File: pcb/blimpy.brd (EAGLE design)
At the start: 250 x 167 mm, 76 parts, among them J1 MICRO-USB, J4 3-PIN SMD, J5 3-PIN SMD, J6 3-PIN SMD, J7 3-PIN SMD, Q1 mmbt2222, Q2 mmbt2222, Q3 DMG3415U, U1 RGB, U10 MAX17048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

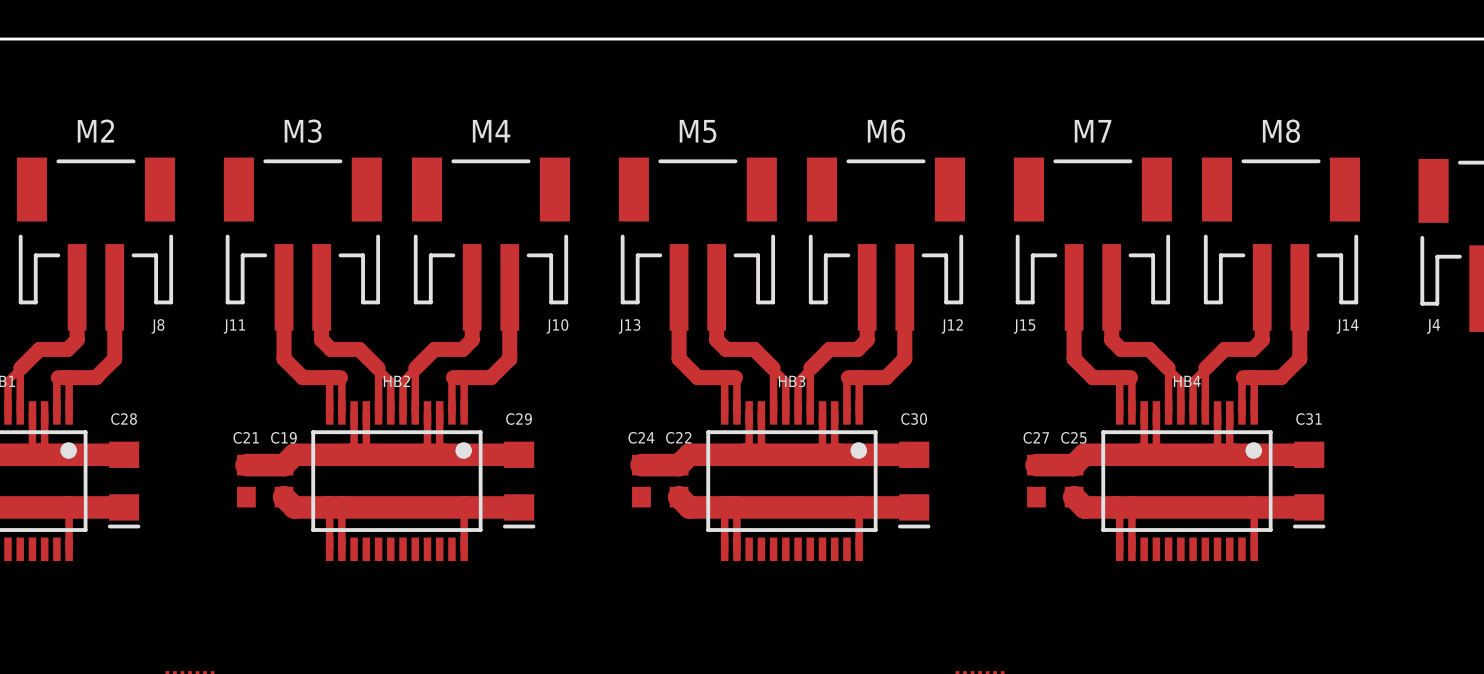
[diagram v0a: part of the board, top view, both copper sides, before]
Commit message: connected adjacent bridges
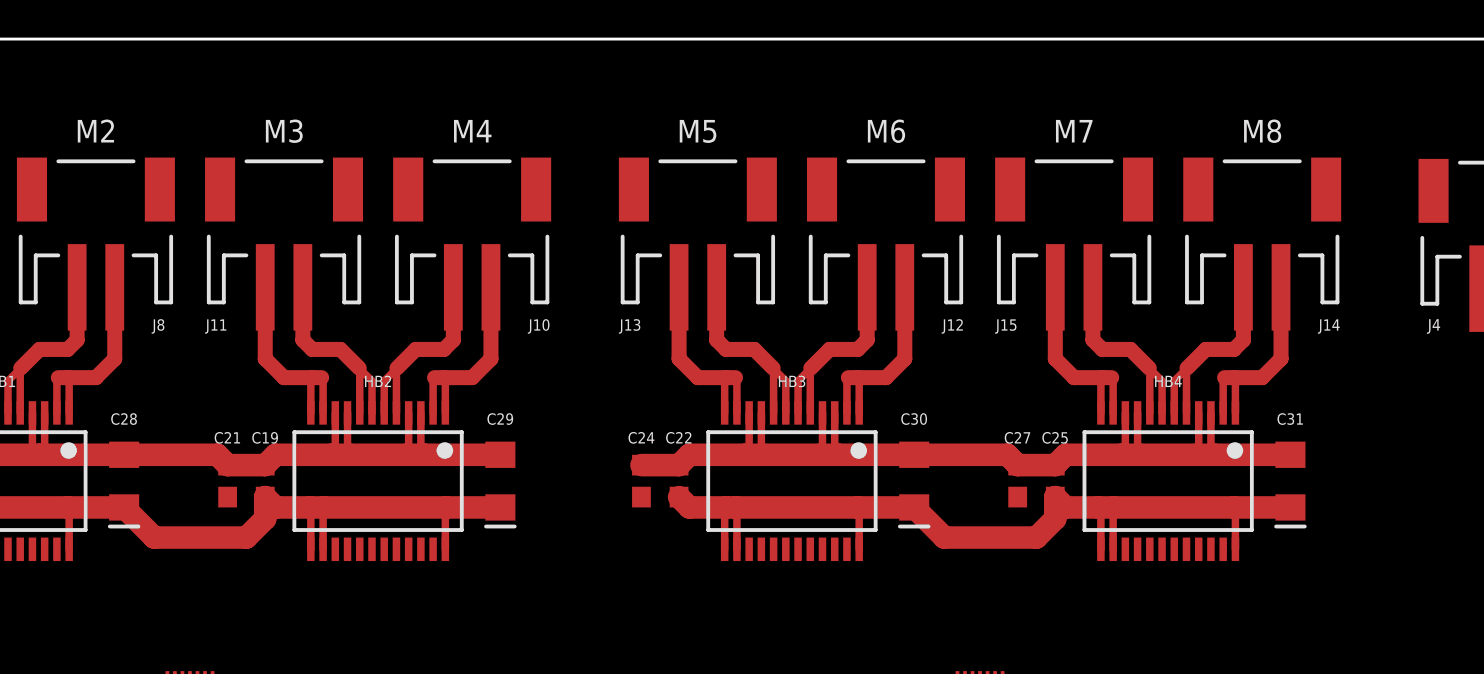
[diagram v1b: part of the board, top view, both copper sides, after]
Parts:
- moved C19 1.00 mm to (55.5, 143.5)
- moved C21 1.00 mm to (53.5, 143.5)
- moved C25 1.00 mm to (97.5, 143.5)
- moved C27 1.00 mm to (95.5, 143.5)
- moved C29 1.00 mm to (68.0, 143.5)
- moved C31 1.00 mm to (110.0, 143.5)
- moved HB2 1.00 mm to (61.5, 143.5)
- moved HB4 1.00 mm to (103.5, 143.5)
- moved J10 1.00 mm to (66.5, 157.5)
- moved J11 1.00 mm to (56.5, 157.5)
- moved J14 1.00 mm to (108.5, 157.5)
- moved J15 1.00 mm to (98.5, 157.5)
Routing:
- net V_BATT: track 77.9 -> 97.4 mm
- net GND: track 95.8 -> 107.3 mm
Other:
- board text added: "Trace Widths for 1oz Copper: Logic: 0.4mm, 15mil (1A) Actors: 0.8mm, 30mil (2A) Battery: 1.2mm, 60mil (3A) Text Sizes Vector, 0.6, 15%"
- board text removed: "Trace Widths for 1oz Copper: Logic: 0.4mm, 15mil (1A) Actors: 0.8mm, 30mil (2A) HBridge: 1.2mm, 45mil (3A) Battery: 1.6mm, 60mil (4A) Text Sizes Vector, 0.6, 15%"

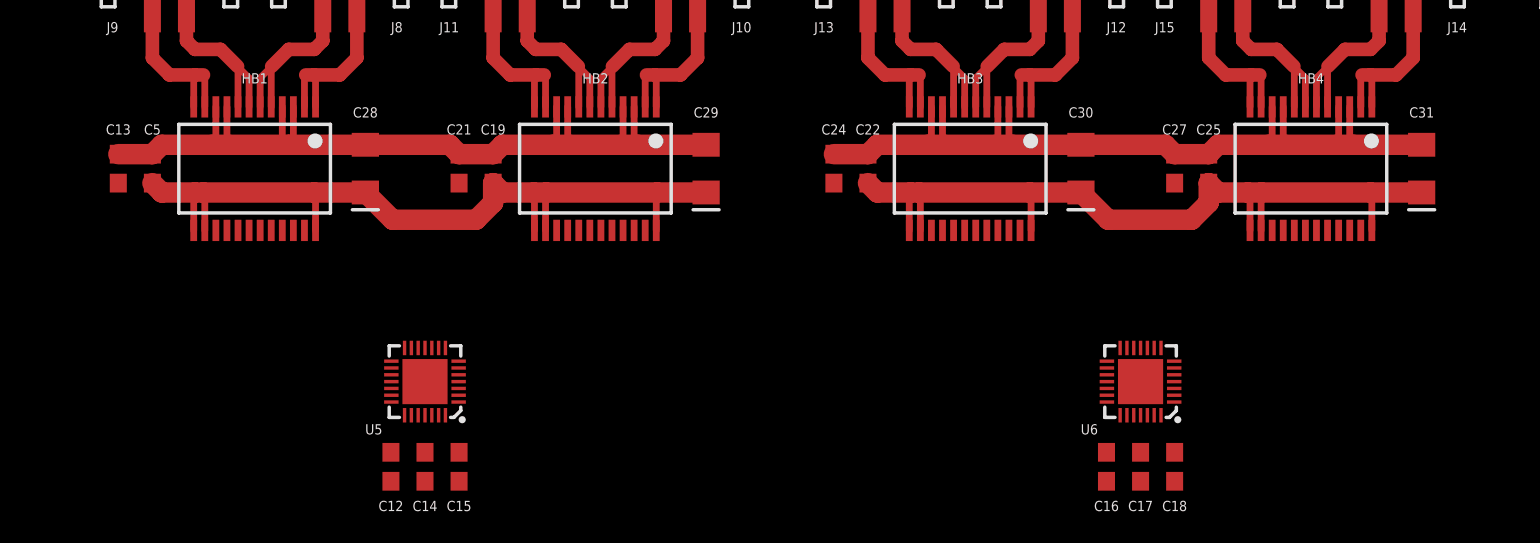
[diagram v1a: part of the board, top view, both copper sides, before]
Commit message: updated hbridge traces and prepared expander
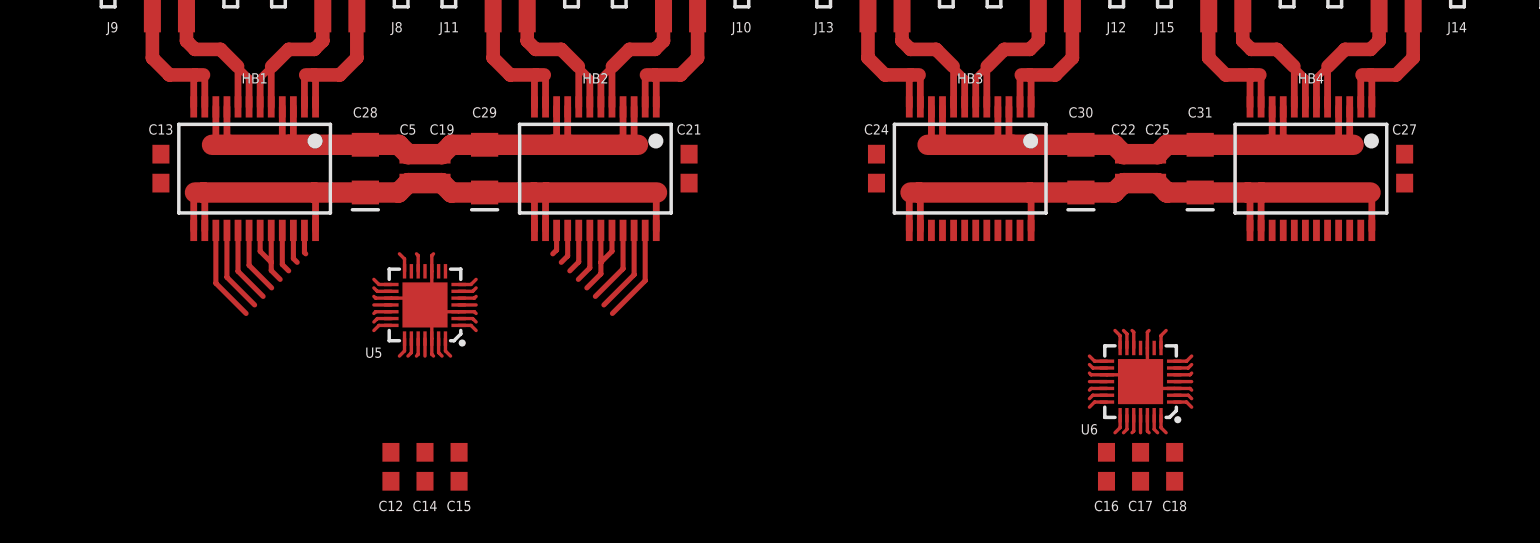
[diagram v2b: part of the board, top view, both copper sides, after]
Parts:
- moved C22 15.0 mm to (92.5, 143.5)
- moved C5 15.0 mm to (50.5, 143.5)
- moved C21 13.5 mm to (67.0, 143.5)
- moved C27 13.5 mm to (109.0, 143.5)
- moved C29 13.0 mm to (55.0, 143.5)
- moved C31 13.0 mm to (97.0, 143.5)
- moved U5 4.50 mm to (51.5, 135.5)
- moved C19 3.00 mm to (52.5, 143.5)
- moved C25 3.00 mm to (94.5, 143.5)
- moved C13 2.50 mm to (36.0, 143.5)
- moved C24 2.50 mm to (78.0, 143.5)
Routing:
- net 3.3V: track 0.00 -> 18.4 mm
- net V_BATT: track 97.4 -> 82.1 mm
- net GND: track 107.3 -> 116.8 mm
- net H2-1: track 0.00 -> 5.67 mm
- net H1-6: track 0.00 -> 5.61 mm
- net H2-2: track 0.00 -> 5.11 mm
- net H1-5: track 0.00 -> 5.05 mm
- net H2-3: track 0.00 -> 4.55 mm
- net H1-4: track 0.00 -> 4.49 mm
- net H2-4: track 0.00 -> 2.59 mm
- net H1-3: track 0.00 -> 2.53 mm
- net SDA: track 0.00 -> 2.13 mm
- net SCL: track 0.00 -> 2.05 mm
- net H2-5: track 0.00 -> 2.03 mm
- net H1-2: track 0.00 -> 1.97 mm
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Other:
- board text added: "Min Trace: 6mil Min Space: 6mil Min Hole: 0.3mm"

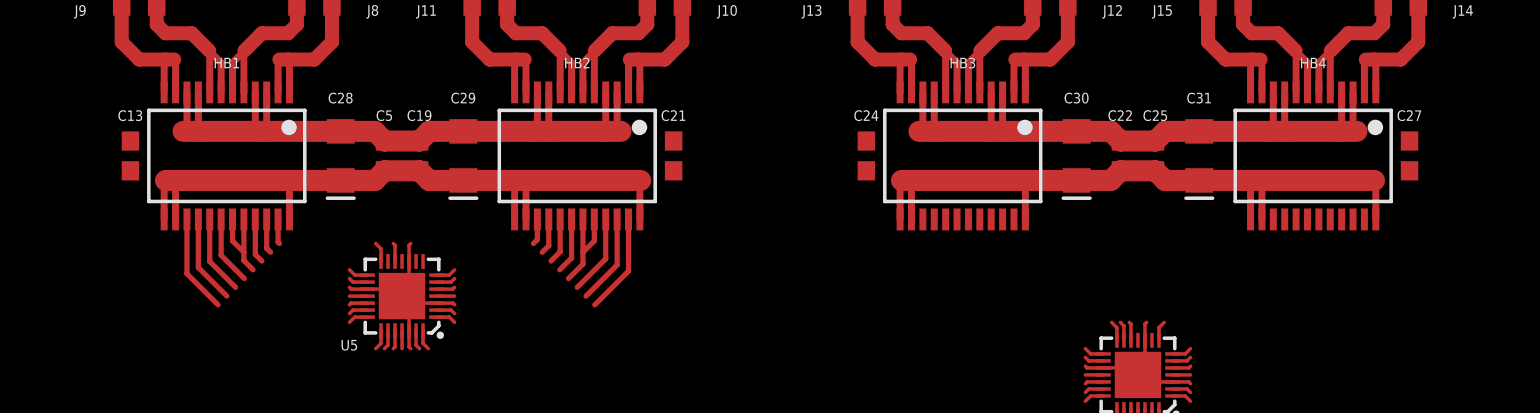
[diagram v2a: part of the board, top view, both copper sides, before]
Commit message: use 0.2mm traces
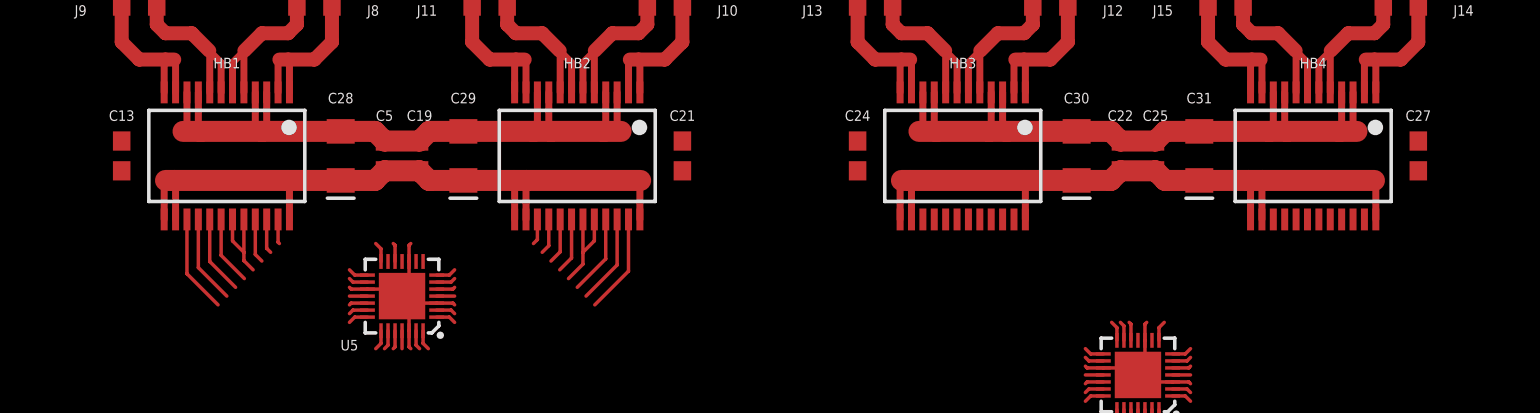
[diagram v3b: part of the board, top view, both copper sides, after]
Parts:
- moved C13 0.50 mm to (35.5, 143.5)
- moved C21 0.50 mm to (67.5, 143.5)
- moved C24 0.50 mm to (77.5, 143.5)
- moved C27 0.50 mm to (109.5, 143.5)
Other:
- board text added: "Trace Widths for 1oz Copper: Logic: 0.2mm, ~8mil Power: 0.4mm, 15mil (1A) Actors: 0.8mm, 30mil (2A) Battery: 1.2mm, 60mil (3A) Text Sizes Vector, 0.6, 15%"
- board text removed: "Trace Widths for 1oz Copper: Logic: 0.4mm, 15mil (1A) Actors: 0.8mm, 30mil (2A) Battery: 1.2mm, 60mil (3A) Text Sizes Vector, 0.6, 15%"

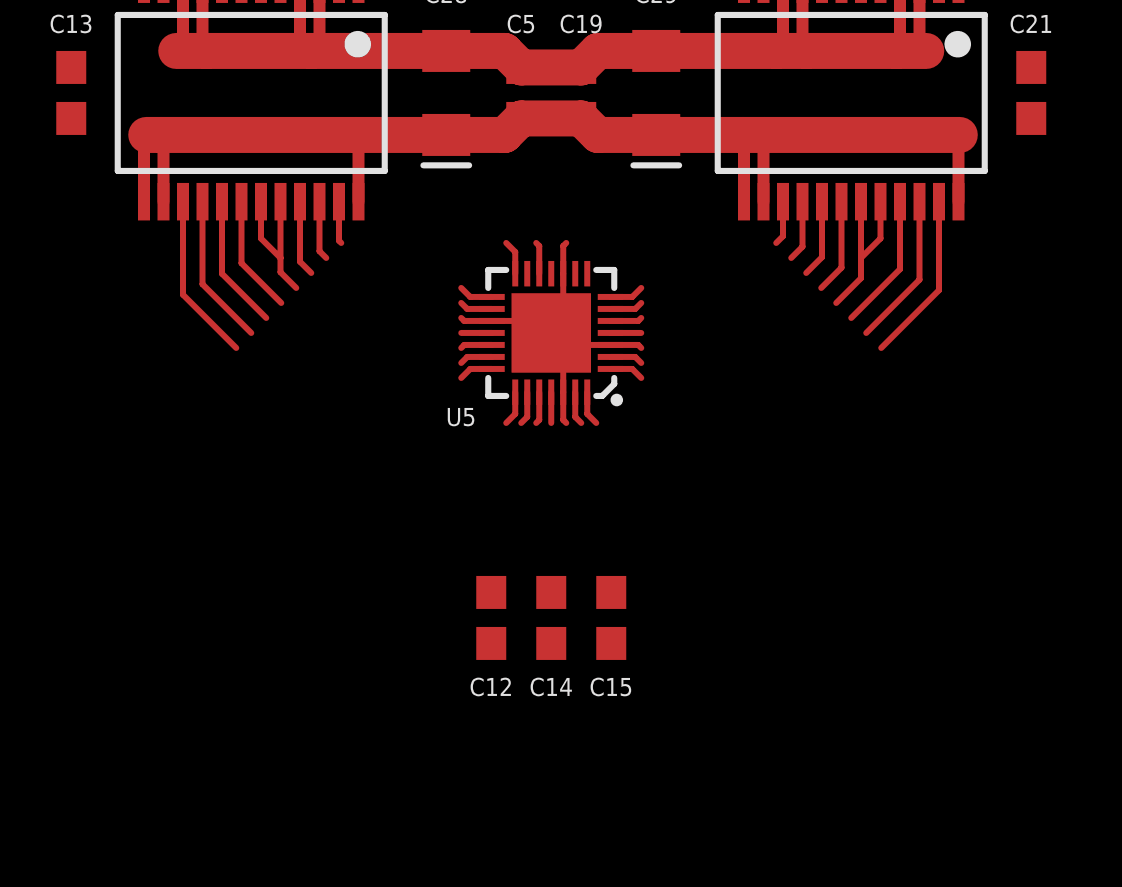
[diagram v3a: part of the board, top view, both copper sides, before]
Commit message: wired io and caps
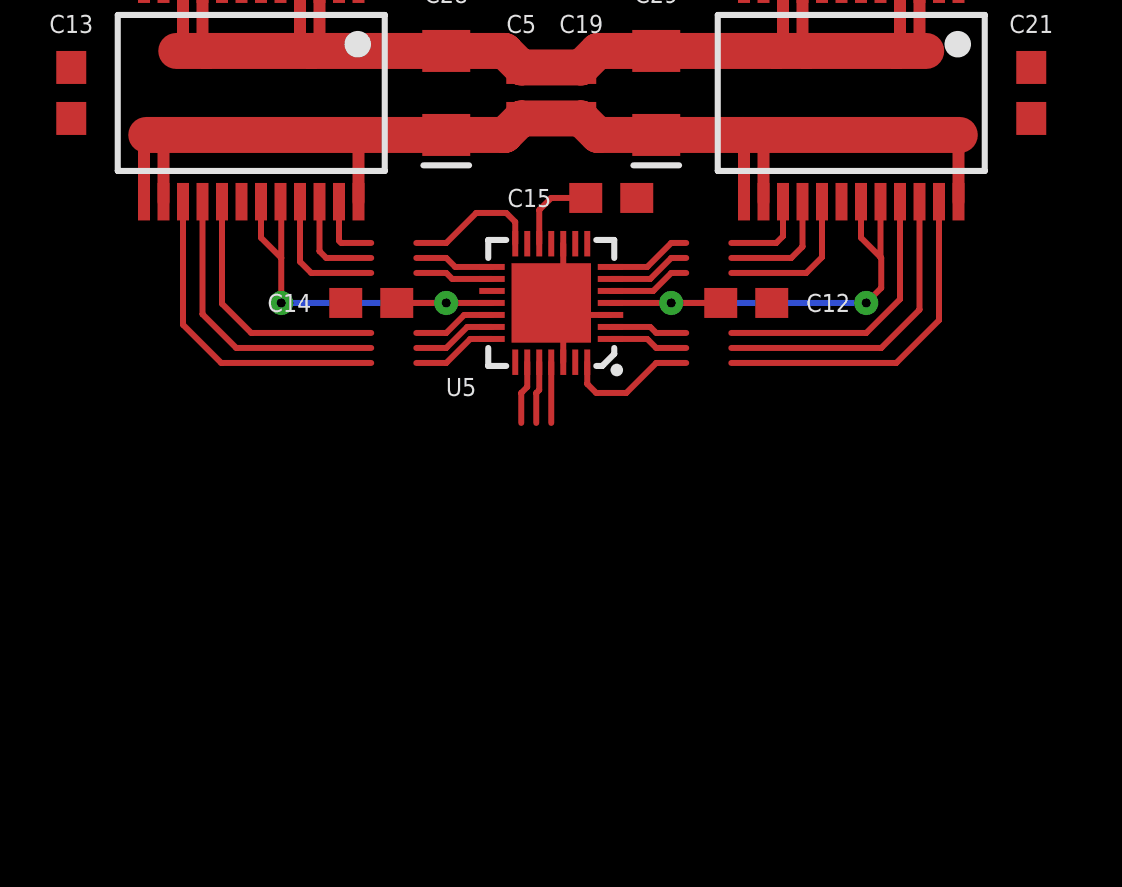
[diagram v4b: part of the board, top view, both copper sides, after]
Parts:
- moved C15 14.0 mm to (53.5, 140.0), turned to 0 degrees
- moved C12 13.5 mm to (58.0, 136.5), turned to 0 degrees
- moved C14 12.1 mm to (45.5, 136.5), turned to 180 degrees
- moved U5 1.00 mm to (51.5, 136.5)
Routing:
- net 3.3V: track 18.4 -> 37.1 mm, vias 0 -> 4
- net GND: track 116.8 -> 103.8 mm
- net H2-1: track 5.67 -> 11.5 mm
- net H2-2: track 5.11 -> 10.4 mm
- net H1-6: track 5.61 -> 10.9 mm
- net H2-3: track 4.55 -> 9.34 mm
- net H1-5: track 5.05 -> 9.84 mm
- net H1-4: track 4.49 -> 8.78 mm
- net 1-2: track 1.15 -> 4.56 mm
- net 1-10: track 1.15 -> 4.56 mm
- net H2-4: track 2.59 -> 5.09 mm
- net H2-5: track 2.03 -> 4.03 mm
- net H1-3: track 2.53 -> 4.53 mm
- net 1-6: track 1.11 -> 2.81 mm
- net 1-14: track 1.11 -> 2.81 mm
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
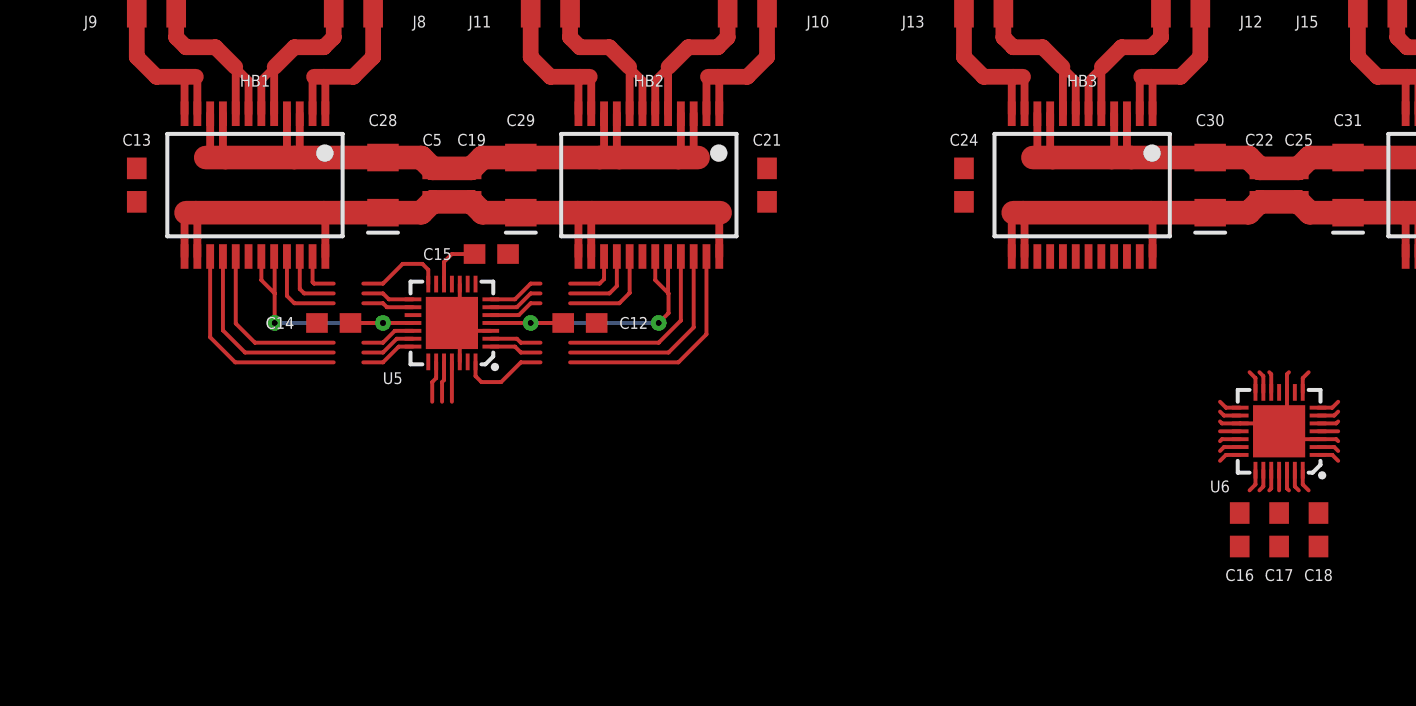
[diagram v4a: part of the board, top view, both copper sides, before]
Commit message: fixed io capacitors
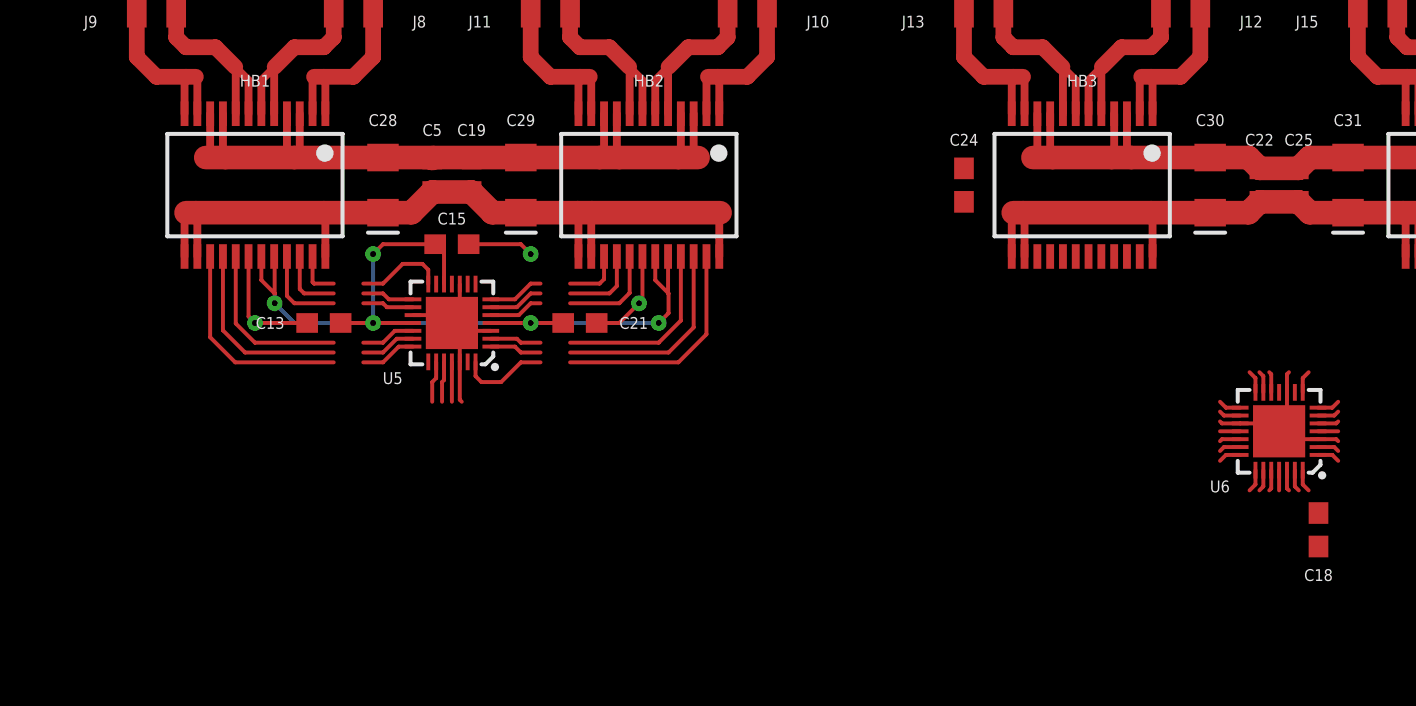
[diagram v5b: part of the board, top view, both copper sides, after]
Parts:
- removed C12, C14, C16, C17: 0.1uF, SparkFun-Capacitors:0603
- moved C13 11.8 mm to (45.0, 136.5), turned to 180 degrees
- moved C21 11.8 mm to (58.0, 136.5), turned to 0 degrees
- moved C15 2.06 mm to (51.5, 140.5)
- moved C19 0.50 mm to (52.5, 144.0)
- moved C5 0.50 mm to (50.5, 144.0)
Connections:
- net 3.3V: no longer C12.1, C14.1, C16.1, C17.1
- net GND: no longer C12.2, C14.2, C16.2, C17.2
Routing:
- net GND: track 103.8 -> 121.5 mm, vias 0 -> 3
- net 3.3V: track 37.1 -> 50.8 mm, vias 4 -> 5
